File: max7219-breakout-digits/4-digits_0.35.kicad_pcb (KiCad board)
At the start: 2 copper layers, 47 x 15.5 mm, 6 parts, among them J1 Conn_02x08_Odd_Even, U1 HDSM-443B_7-Segment_2_Digit, U2 HDSM-443B_7-Segment_2_Digit

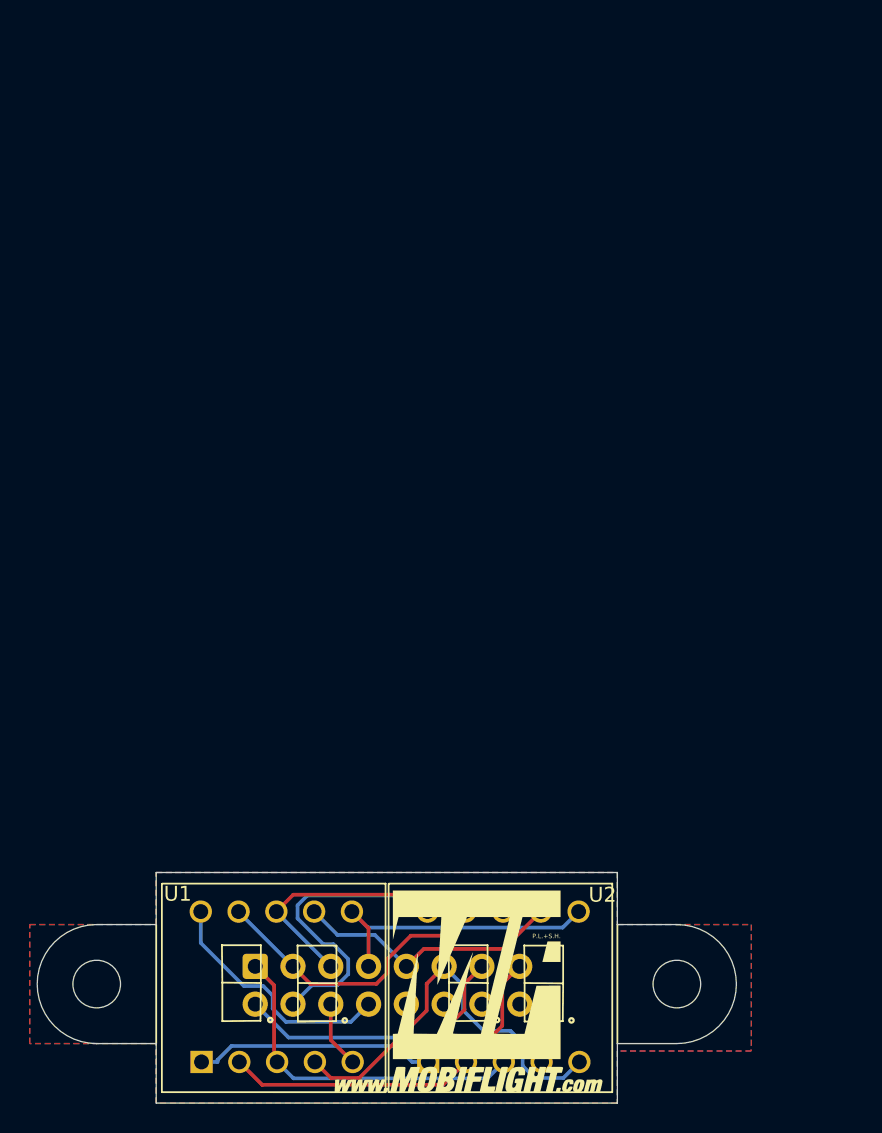
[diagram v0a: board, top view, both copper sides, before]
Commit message: add .35 symbols and footprints, rework 3 and 4 digit 0.35
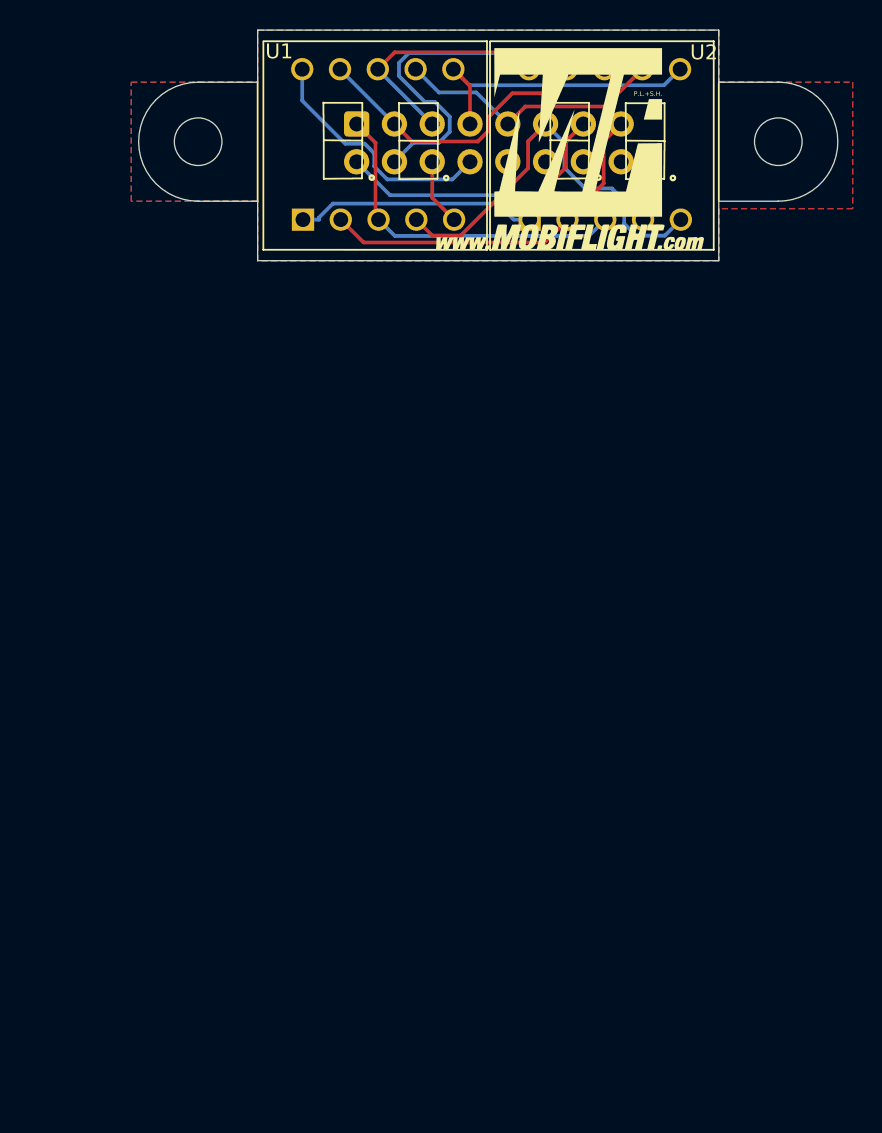
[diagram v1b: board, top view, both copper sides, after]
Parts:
- moved G*** 57.0 mm to (100.7, 59.3)
- moved J1 57.0 mm to (86.4, 57.7)
- moved REF1 57.0 mm to (75.7, 58.8)
- moved REF2 57.0 mm to (114.7, 58.8)
- moved U1 57.0 mm to (91.8, 58.9)
- moved U2 57.0 mm to (107.0, 58.9)

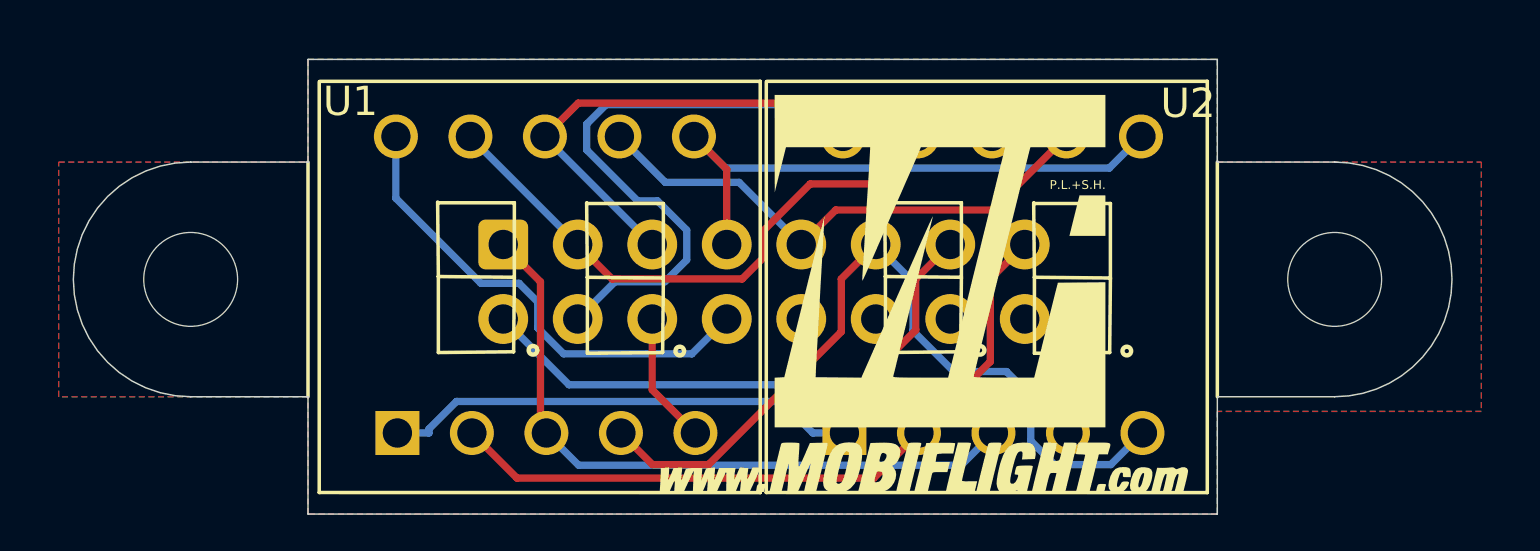
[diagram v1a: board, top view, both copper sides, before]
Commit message: rotate IDC on 0.28 displays, plated mounting holes for 0.35 displays, set version for 0.35 displays
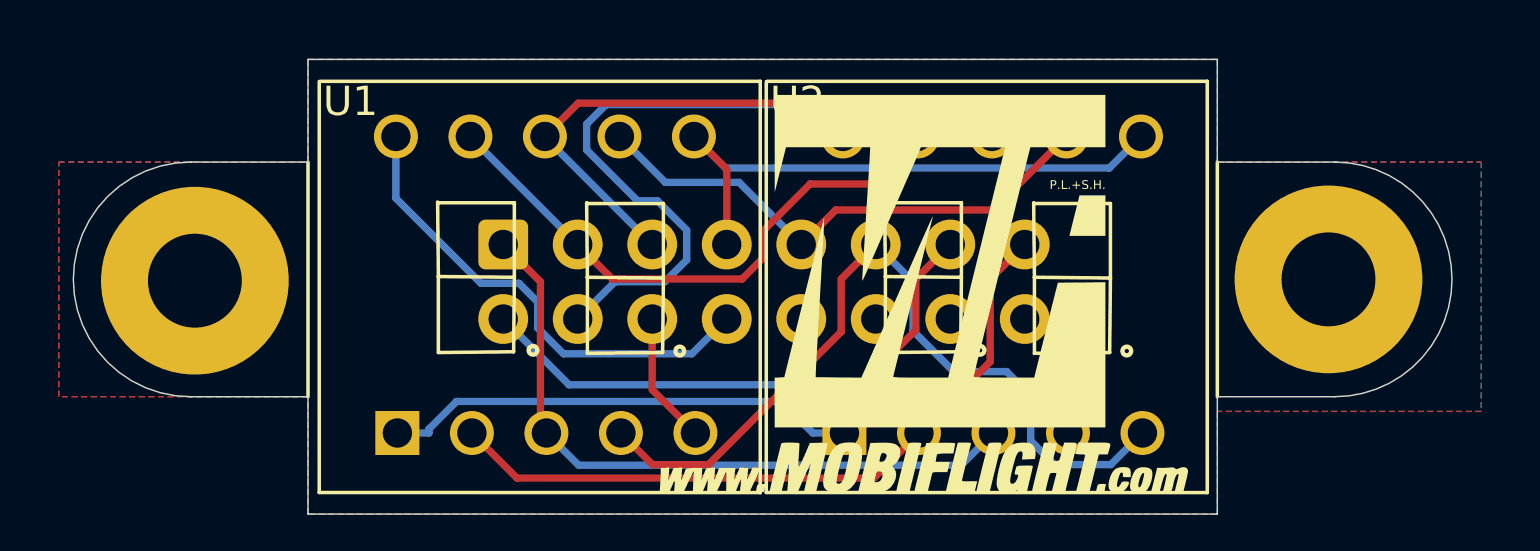
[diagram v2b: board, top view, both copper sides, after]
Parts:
- removed REF1, REF2: MountingHole_3.2mm_M3, MountingHole:MountingHole_3.2mm_M3
- added H1: MountingHole 3.2mm, MountingHole:MountingHole_3.2mm_M3_Pad, F.Cu at (75.9, 58.9)
- added H2: MountingHole 3.2mm, MountingHole:MountingHole_3.2mm_M3_Pad, F.Cu at (114.5, 58.8)
- U1, U2: footprint Display_7Segment:SN42056STH -> MobiFlight:STH_7_2 Digits_0.35_CC
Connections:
- J1 pad 10: (no net) -> unconnected-(J1-Pin_10-Pad10)
- J1 pad 12: (no net) -> unconnected-(J1-Pin_12-Pad12)
- J1 pad 14: (no net) -> unconnected-(J1-Pin_14-Pad14)
- J1 pad 16: (no net) -> unconnected-(J1-Pin_16-Pad16)
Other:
- board text added: "4 Digit Module ${REVISION}"
- board text removed: "4 Digit Module V1.0"
